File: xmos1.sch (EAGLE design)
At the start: 3 parts

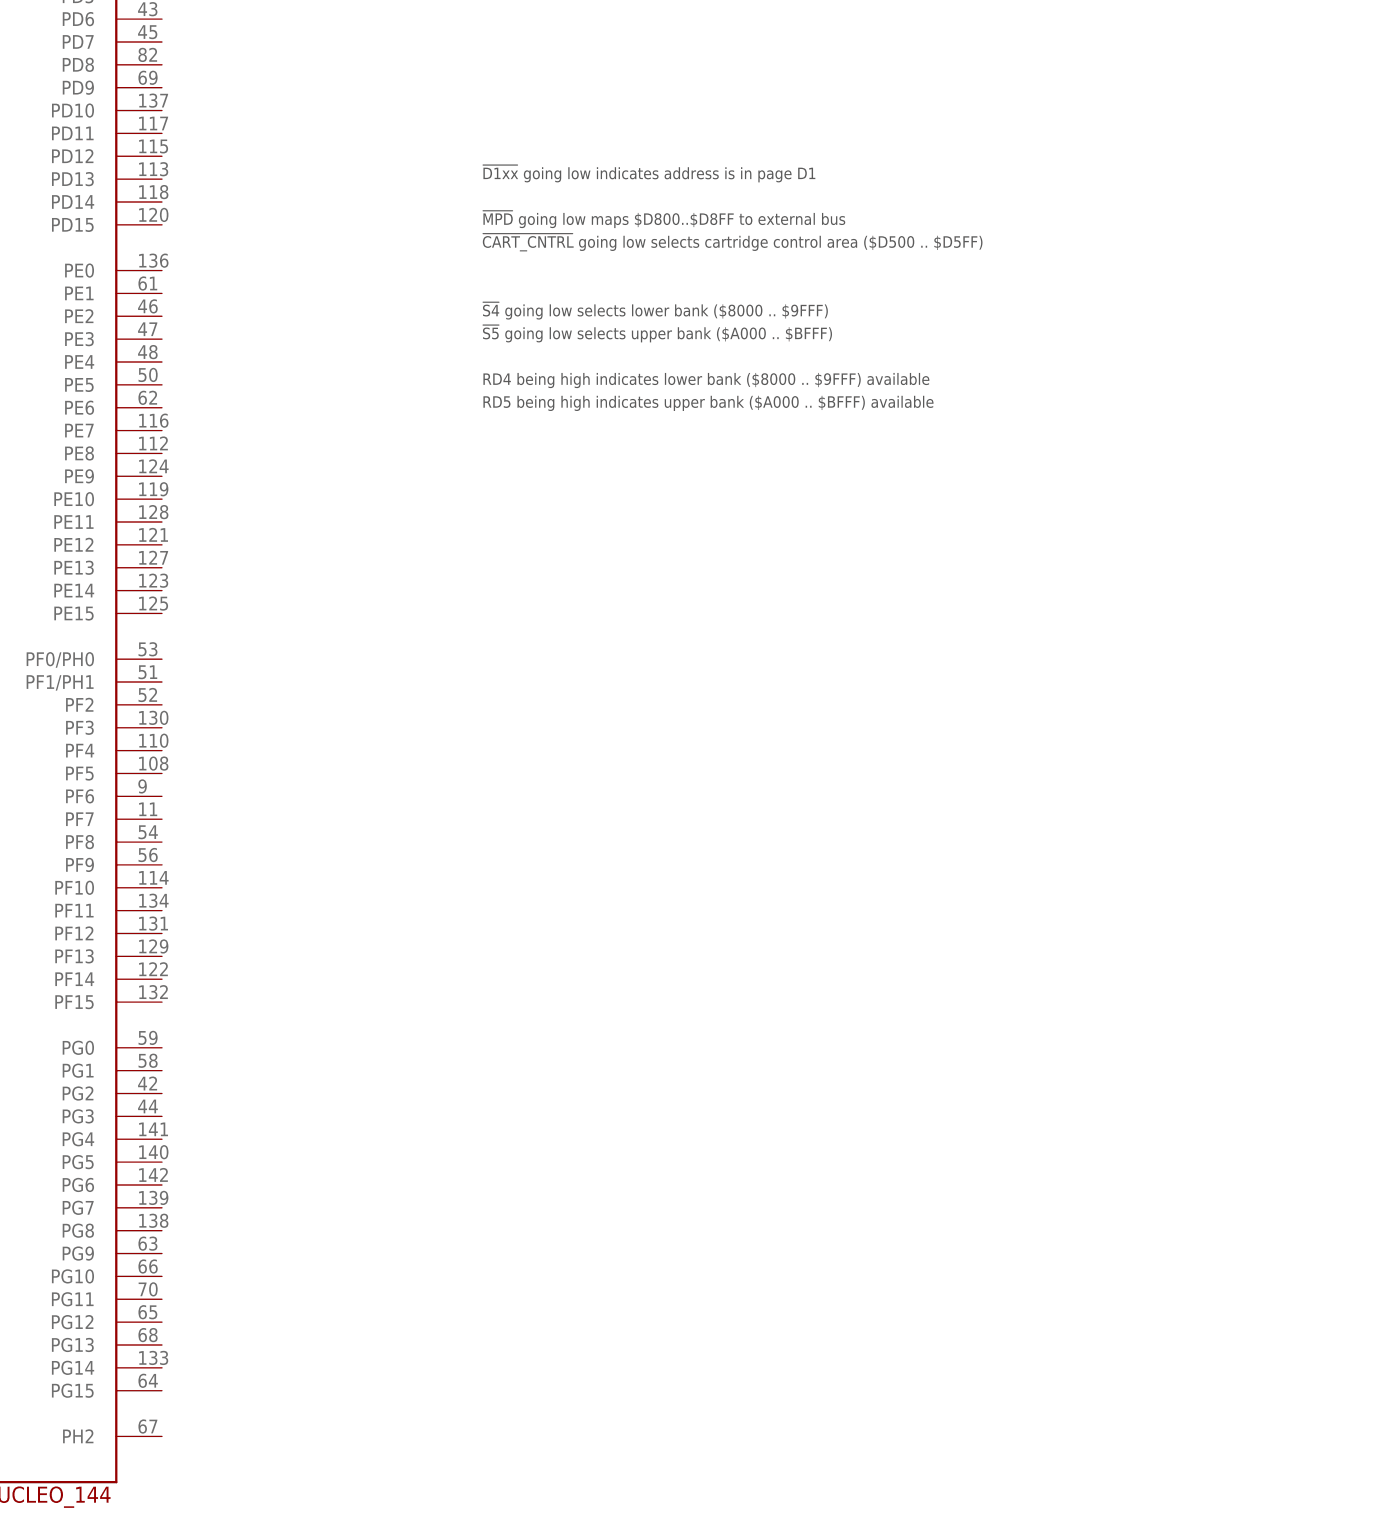
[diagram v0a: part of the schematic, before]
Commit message: Add the two spare ports to the top. Just needs power now
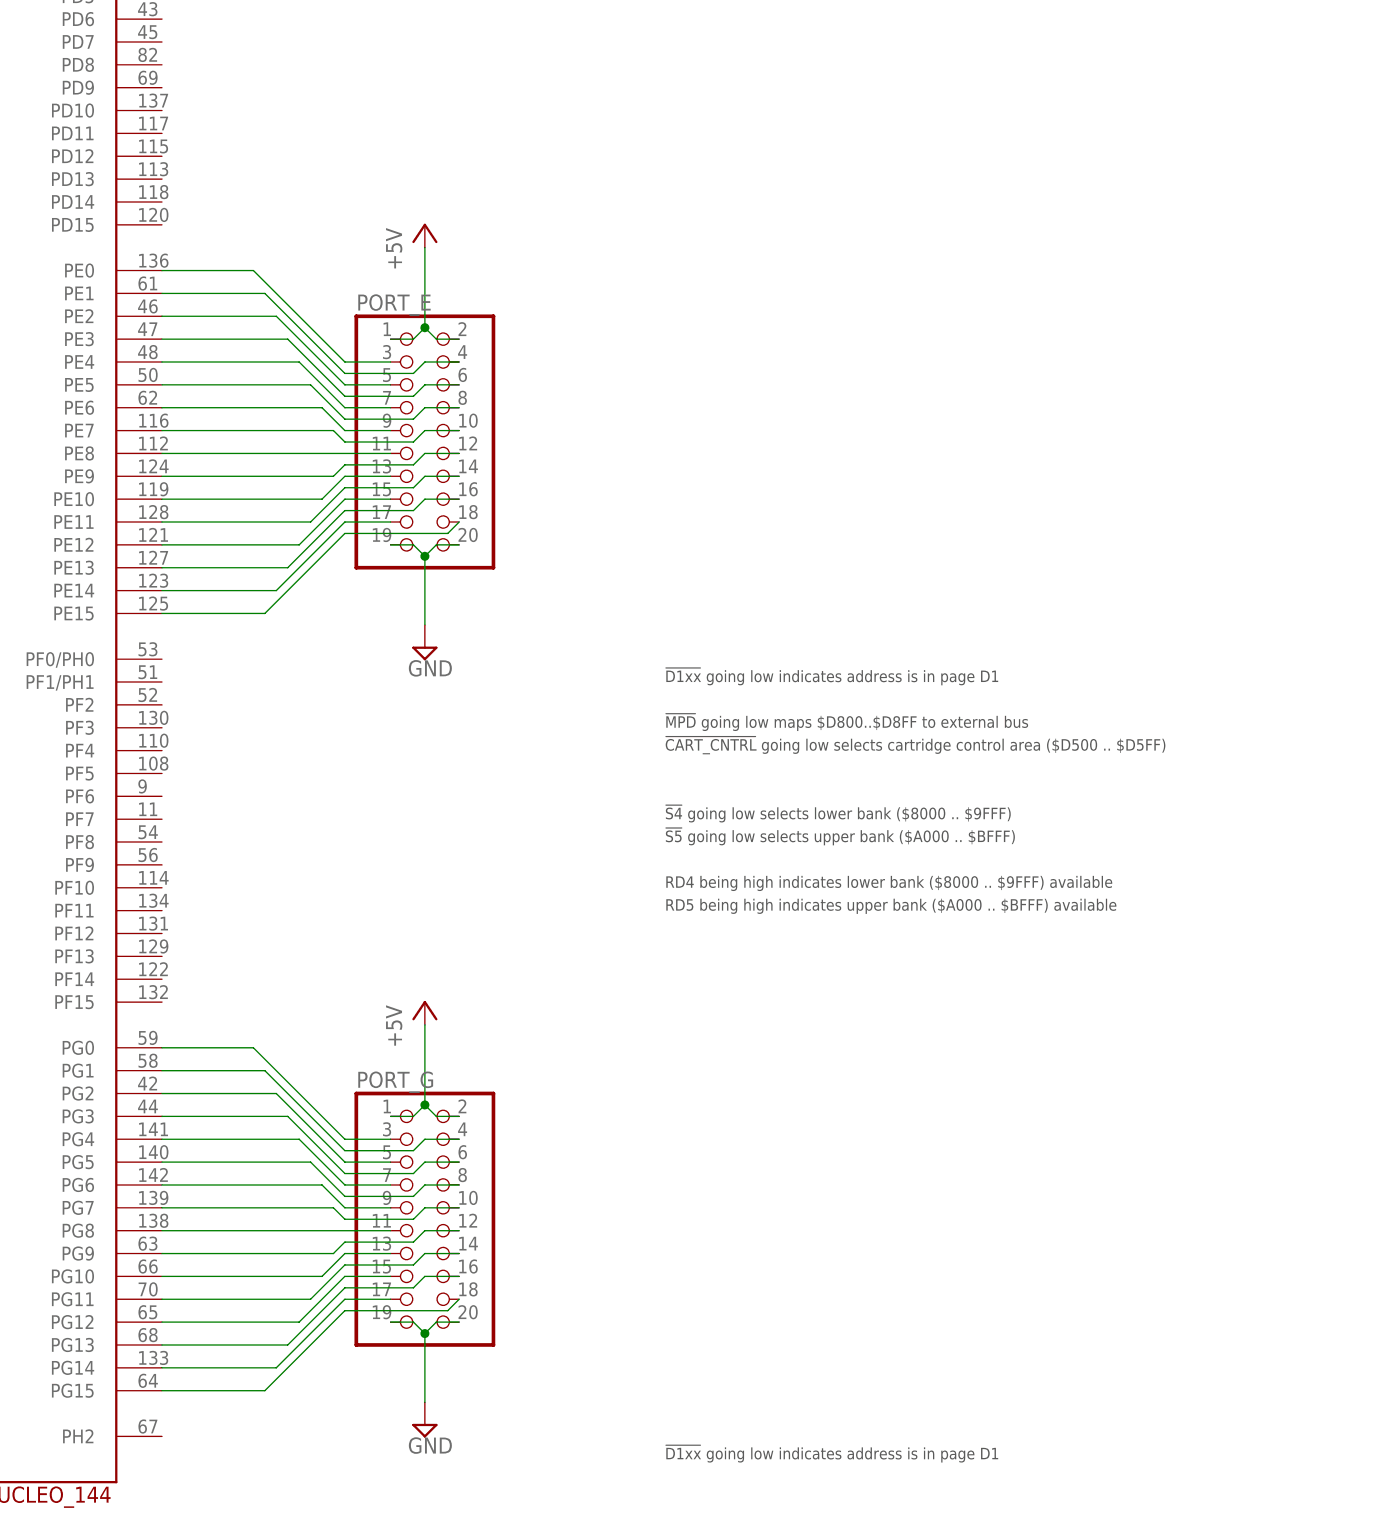
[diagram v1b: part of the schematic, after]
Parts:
- added PORT_E, PORT_G: (no value), pinhead:PINHD-2X10
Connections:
- new net N$10: PORT_E.10, U$1.PE7@CN12_44
- new net N$11: PORT_E.11, U$1.PE8@CN12_40
- new net N$12: PORT_E.12, U$1.PE9@CN12_52
- new net N$13: PORT_E.13, U$1.PE10@CN12_47
- new net N$14: PORT_E.14, U$1.PE11@CN12_56
- new net N$15: PORT_E.15, U$1.PE12@CN12_49
- new net N$16: PORT_E.16, U$1.PE13@CN12_55
- new net N$17: PORT_E.17, U$1.PE14@CN12_51
- new net N$18: PORT_E.18, U$1.PE15@CN12_53
- new net N$19: PORT_G.3, U$1.PG0@CN11_59
- new net N$20: PORT_G.4, U$1.PG1@CN11_58
- new net N$21: PORT_G.5, U$1.PG2@CN11_42
- new net N$22: PORT_G.6, U$1.PG3@CN11_44
- new net N$23: PORT_G.7, U$1.PG4@CN12_69
- new net N$24: PORT_G.8, U$1.PG5@CN12_68
- new net N$25: PORT_G.9, U$1.PG6@CN12_70
- new net N$26: PORT_G.11, U$1.PG8@CN12_66
- new net N$28: PORT_G.12, U$1.PG9@CN11_63
- new net N$29: PORT_G.13, U$1.PG10@CN11_66
- new net N$3: PORT_E.3, U$1.PE0@CN12_64
- new net N$30: PORT_G.14, U$1.PG11@CN11_70
- new net N$31: PORT_G.15, U$1.PG12@CN11_65
- new net N$32: PORT_G.16, U$1.PG13@CN11_68
- new net N$33: PORT_G.17, U$1.PG14@CN12_61
- new net N$34: PORT_G.18, U$1.PG15@CN11_64
- new net N$4: PORT_E.4, U$1.PE1@CN11_61
- new net N$5: PORT_E.5, U$1.PE2@CN11_46
- new net N$6: PORT_E.6, U$1.PE3@CN11_47
- new net N$7: PORT_E.7, U$1.PE4@CN11_48
- new net N$8: PORT_E.8, U$1.PE5@CN11_50
- new net N$9: PORT_E.9, U$1.PE6@CN11_62
- new net PORT_G: PORT_G.10, U$1.PG7@CN12_67
- net +5V: now also PORT_E.1, PORT_E.2, PORT_G.1, PORT_G.2
- net GND: now also PORT_E.19, PORT_E.20, PORT_G.19, PORT_G.20

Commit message: Add a voltage-regulator option for external power, and clean up the board a bit
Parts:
- added C1: 4.7uF, rcl:C-EUC0603
- added C2: 1uF, rcl:C-EUC0603
- added J1: POWER_JACKPTH, SparkFun-Connectors:POWER_JACKPTH
- added U$3: LD1117, sjg-power:LD1117
- renumbered U$2 to CARTRIDGE_SLOT
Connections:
- new net N$27: C2.2, J1.PWR, U$3.VIN
- net GND: now also C1.1, C2.1, J1.GND, J1.GNDBREAK, U$3.GND
- net N$1: now also C1.2, U$3.TAB, U$3.VOUT
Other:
- note added: "311-1455-1-ND"
- note added: "587-1248-1-ND"
- note added: "Ports E and G solely for future expansion"
- moved on the sheet: JP1
